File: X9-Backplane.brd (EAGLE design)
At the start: 122.1 x 89.3 mm, 11 parts

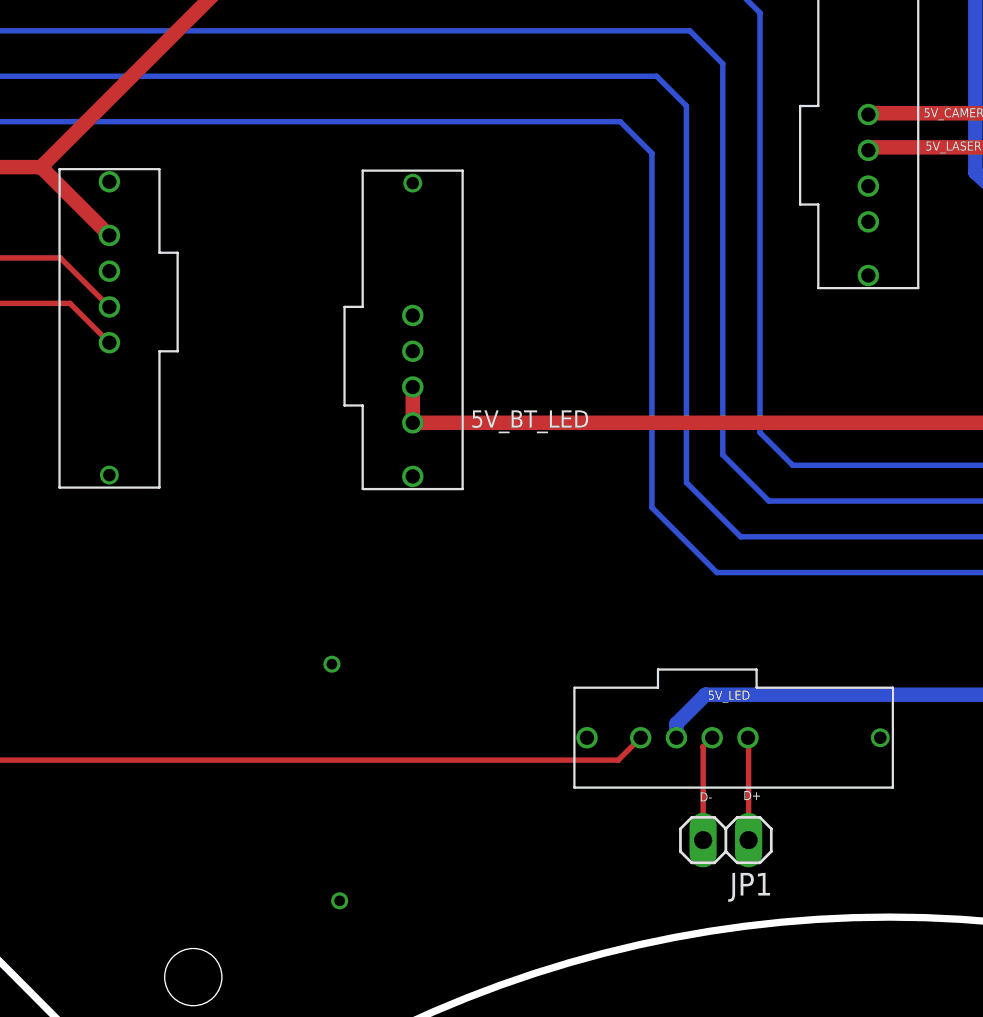
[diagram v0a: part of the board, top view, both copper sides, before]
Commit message: added debugging pins
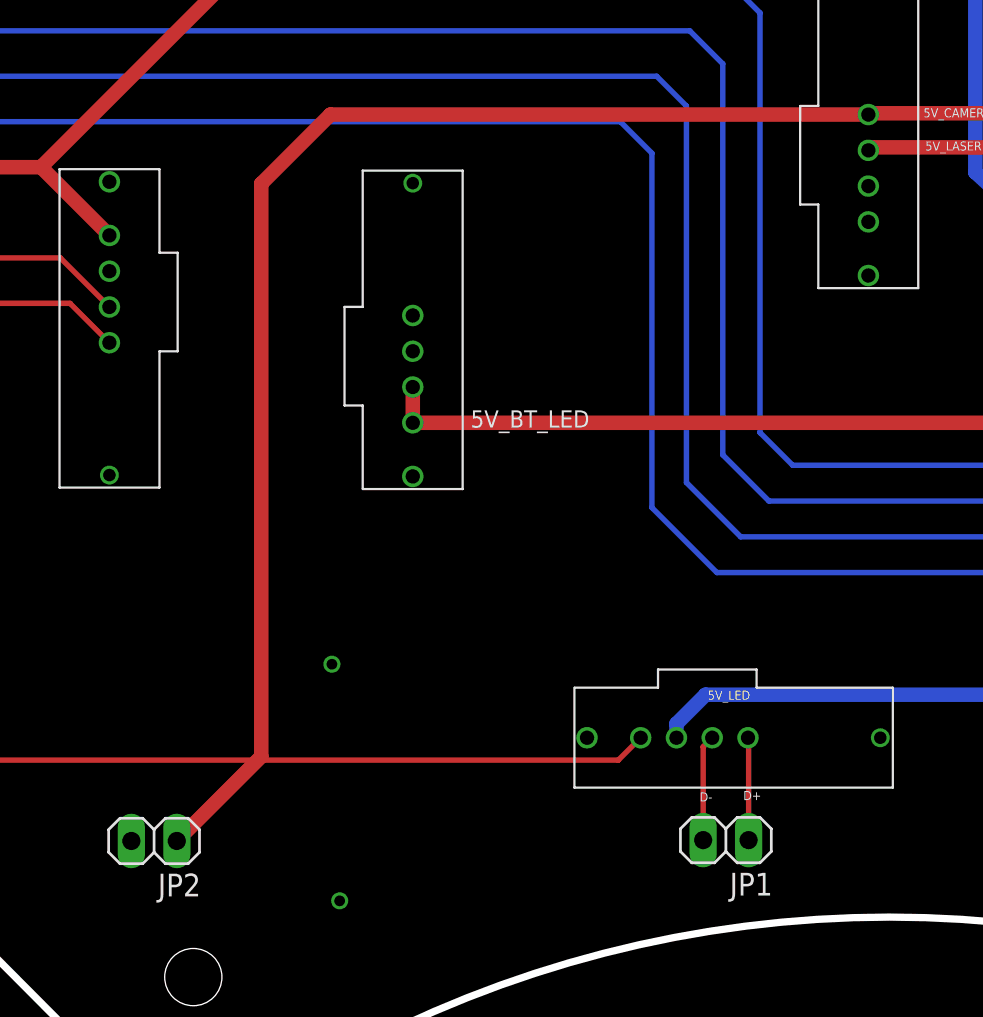
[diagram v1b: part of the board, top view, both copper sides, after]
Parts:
- added JP2: (no value), pinhead:1X02
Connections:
- net 5V_CAMERA_TUBE: now also JP2.1
- net GND: now also JP2.2
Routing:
- net 5V_CAMERA_TUBE: track 68.2 -> 142.5 mm
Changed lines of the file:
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@@
 <text x="103.8" y="63.9" size="1.778" layer="22" rot="MR0">MAIN_POWER</text>
 <wire x1="121.510525" y1="62.19769375" x2="121.485125" y2="12.1368625" width="0.4064" layer="20"/>
-<text x="41.8248" y="27.3338" size="1.778" layer="22" rot="MR0">BT_POWER</text>
-<text x="22.5962" y="27.0222" size="1.778" layer="22" rot="MR0">BT_SIGNAL</text>
-<text x="69.881" y="25.9566" size="1.778" layer="22" rot="MR0">CAMPOW</text>
+<text x="41.266" y="23.5492" size="1.778" layer="22" rot="MR0">BT_POWER</text>
+<text x="22.774" y="23.7964" size="1.778" layer="22" rot="MR0">BT_SIGNAL</text>
+<text x="65.9186" y="35.0244" size="1.778" layer="22" rot="MR0">CAMPOW</text>
 <text x="71.1874" y="11.2268" size="1.778" layer="22" rot="MR0">CAMDATA</text>
 <text x="41.2954" y="78.4302" size="1.778" layer="22" rot="MR0">S_PIEZO</text>
@@
 <element name="JP1" library="pinhead" package="1X02" value="" x="52.0652" y="6.5744" rot="R180"/>
 <element name="PS" library="con-hirose-df13" package="DF13-4P-1.25DSA" value="DF13-4P-1.25DSA" x="61.018" y="77.5974" rot="R90"/>
+<element name="JP2" library="pinhead" package="1X02" value="" x="20.0914" y="6.5278" rot="R180"/>
 </elements>
 <signals>
@@
 <via x="20.805134375" y="58.000896875" extent="1-16" drill="0.6"/>
 <via x="16.187415625" y="69.552815625" extent="1-16" drill="0.6"/>
+<contactref element="JP2" pad="2"/>
 </signal>
 <signal name="N$11">
@@
 <wire x1="68.4022" y1="47.2186" x2="60.105" y2="47.2186" width="0.8128" layer="1"/>
 <wire x1="60.105" y1="47.2186" x2="60.033759375" y2="47.147359375" width="0.8128" layer="1"/>
+<contactref element="JP2" pad="1"/>
+<wire x1="60.033759375" y1="47.147359375" x2="29.951559375" y2="47.147359375" width="0.8128" layer="1"/>
+<wire x1="29.951559375" y1="47.147359375" x2="26.0858" y2="43.2816" width="0.8128" layer="1"/>
+<wire x1="26.0858" y1="43.2816" x2="26.0858" y2="11.2522" width="0.8128" layer="1"/>
+<wire x1="26.0858" y1="11.2522" x2="21.3614" y2="6.5278" width="0.8128" layer="1"/>
 </signal>
 <signal name="5V_BT_LED">

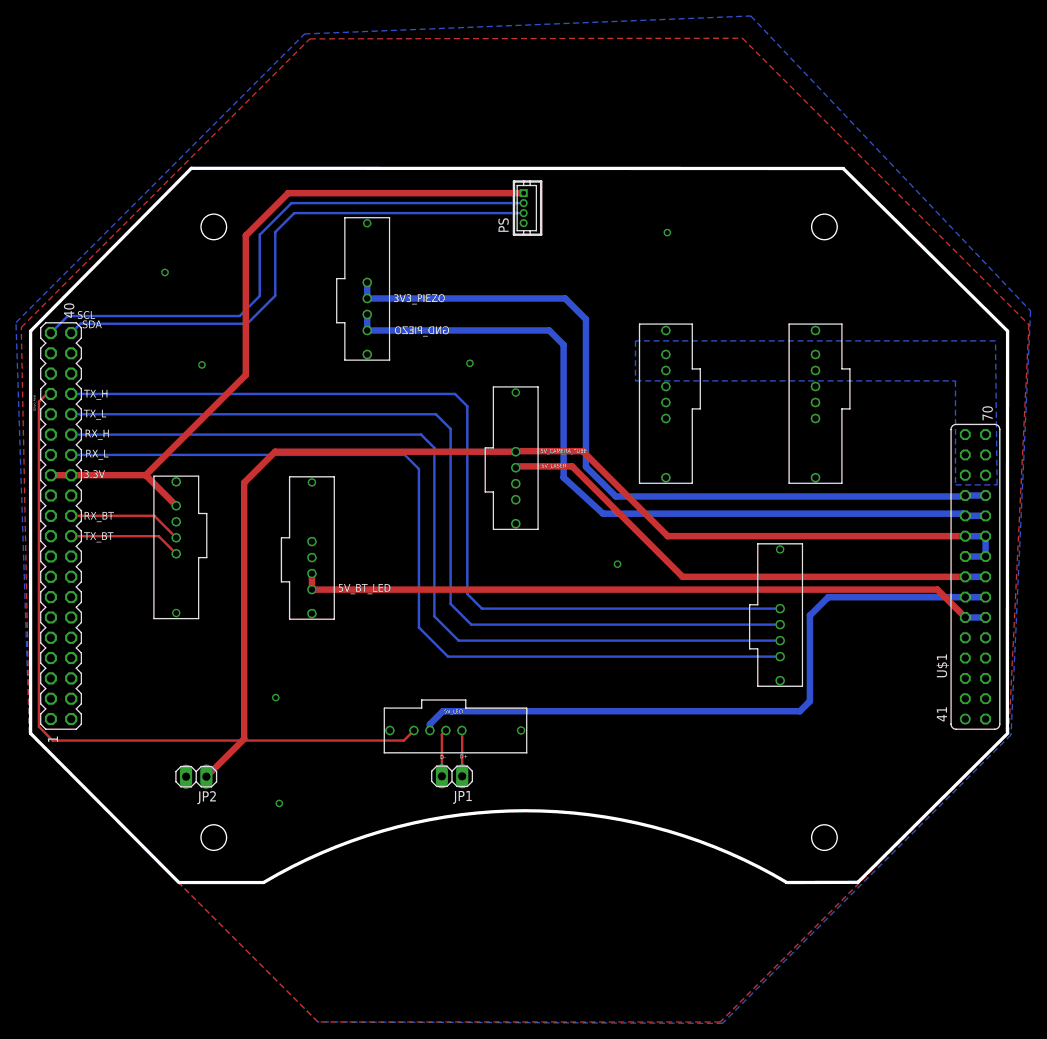
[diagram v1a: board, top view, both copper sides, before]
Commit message: Fixed routing issue
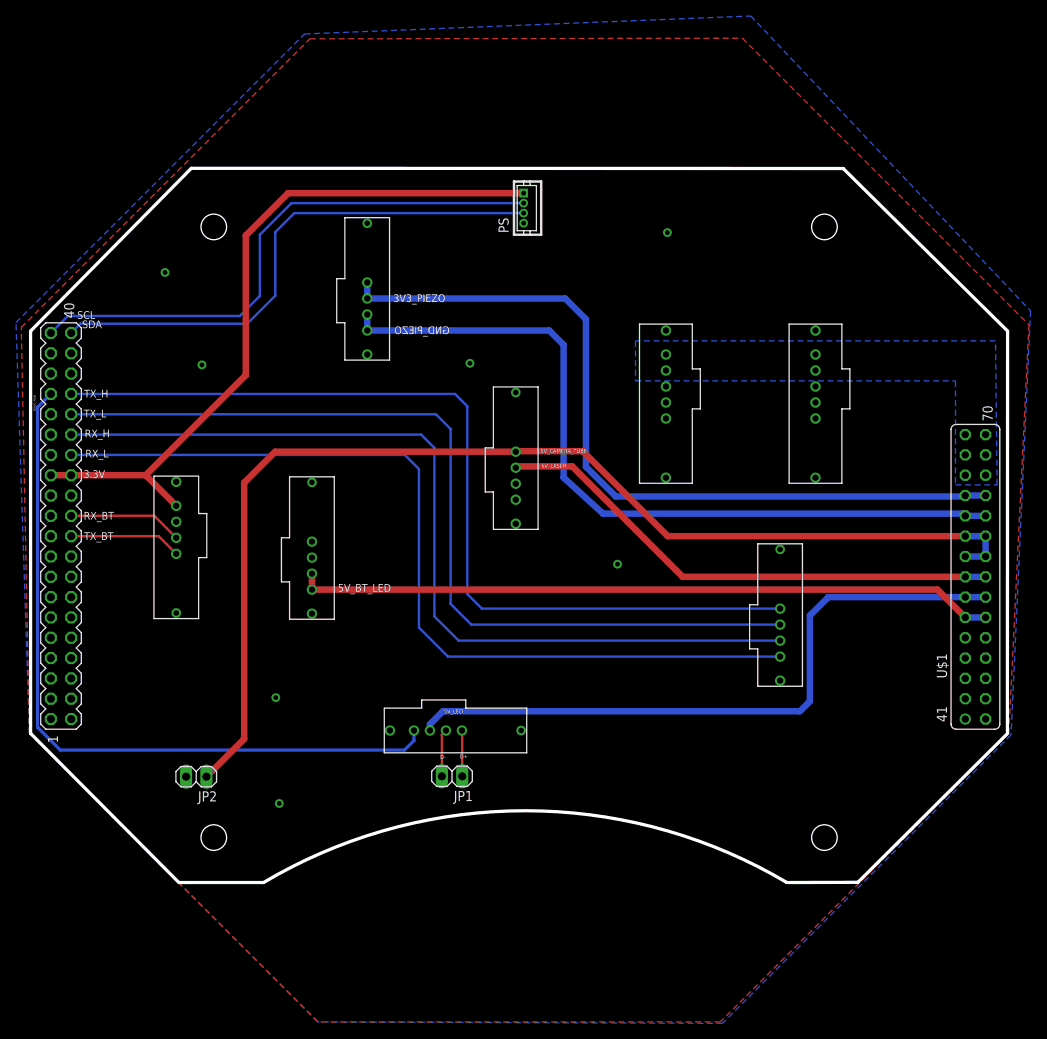
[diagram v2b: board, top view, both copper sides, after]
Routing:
- net SERVO_PWM: track 90.6 -> 92.3 mm
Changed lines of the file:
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@@
 <setting verticaltext="up"/>
 </settings>
-<grid distance="1" unitdist="mil" unit="mil" style="lines" multiple="1" display="yes" altdistance="0.025" altunitdist="inch" altunit="inch"/>
+<grid distance="10" unitdist="mil" unit="mil" style="lines" multiple="1" display="yes" altdistance="0.025" altunitdist="inch" altunit="inch"/>
 <layers>
 <layer number="1" name="Top" color="4" fill="1" visible="yes" active="yes"/>
@@
 </class>
 </classes>
-<designrules name="LaenPCBOrder">
-<description language="de">&lt;b&gt;EAGLE Design Rules&lt;/b&gt;
+<designrules name="GoldPhoenix">
+<description language="en">
+&lt;b&gt;Gold Phoenix PCB Design Rules&lt;/b&gt;
 &lt;p&gt;
-Die Standard-Design-Rules sind so gewählt, dass sie für
-die meisten Anwendungen passen. Sollte ihre Platine
-besondere Anforderungen haben, treffen Sie die erforderlichen
-Einstellungen hier und speichern die Design Rules unter
-einem neuen Namen ab.</description>
-<description language="en">&lt;b&gt;Laen's PCB Order Design Rules&lt;/b&gt;
-&lt;p&gt;
-Please make sure your boards conform to these design rules.</description>
+Created by Nick Molo for the Purdue IEEE ROV Team
+</description>
 <param name="layerSetup" value="(1*16)"/>
-<param name="mtCopper" value="0.0356mm 0.0356mm 0.0356mm 0.0356mm 0.0356mm 0.0356mm 0.0356mm 0.0356mm 0.0356mm 0.0356mm 0.0356mm 0.0356mm 0.0356mm 0.0356mm 0.0356mm 0.0356mm"/>
-<param name="mtIsolate" value="1.5011mm 0.1499mm 0.2007mm 0.1499mm 0.2007mm 0.1499mm 0.2007mm 0.1499mm 0.2007mm 0.1499mm 0.2007mm 0.1499mm 0.2007mm 0.1499mm 0.2007mm"/>
-<param name="mdWireWire" value="6mil"/>
-<param name="mdWirePad" value="6mil"/>
-<param name="mdWireVia" value="6mil"/>
-<param name="mdPadPad" value="6mil"/>
-<param name="mdPadVia" value="6mil"/>
-<param name="mdViaVia" value="6mil"/>
-<param name="mdSmdPad" value="6mil"/>
-<param name="mdSmdVia" value="6mil"/>
-<param name="mdSmdSmd" value="6mil"/>
+<param name="mtCopper" value="0.035mm 0.035mm 0.035mm 0.035mm 0.035mm 0.035mm 0.035mm 0.035mm 0.035mm 0.035mm 0.035mm 0.035mm 0.035mm 0.035mm 0.035mm 0.035mm"/>
+<param name="mtIsolate" value="1.5mm 0.15mm 0.2mm 0.15mm 0.2mm 0.15mm 0.2mm 0.15mm 0.2mm 0.15mm 0.2mm 0.15mm 0.2mm 0.15mm 0.2mm"/>
+<param name="mdWireWire" value="7mil"/>
+<param name="mdWirePad" value="7mil"/>
+<param name="mdWireVia" value="7mil"/>
+<param name="mdPadPad" value="7mil"/>
+<param name="mdPadVia" value="7mil"/>
+<param name="mdViaVia" value="7mil"/>
+<param name="mdSmdPad" value="7mil"/>
+<param name="mdSmdVia" value="7mil"/>
+<param name="mdSmdSmd" value="7mil"/>
 <param name="mdViaViaSameLayer" value="8mil"/>
 <param name="mnLayersViaInSmd" value="2"/>
-<param name="mdCopperDimension" value="15mil"/>
-<param name="mdDrill" value="6mil"/>
+<param name="mdCopperDimension" value="10mil"/>
+<param name="mdDrill" value="8mil"/>
 <param name="mdSmdStop" value="0mil"/>
-<param name="msWidth" value="6mil"/>
-<param name="msDrill" value="13mil"/>
-<param name="msMicroVia" value="13mil"/>
+<param name="msWidth" value="7mil"/>
+<param name="msDrill" value="10mil"/>
+<param name="msMicroVia" value="9.99mm"/>
 <param name="msBlindViaRatio" value="0.5"/>
 <param name="rvPadTop" value="0.25"/>
@@
 <param name="rvMicroViaOuter" value="0.25"/>
 <param name="rvMicroViaInner" value="0.25"/>
-<param name="rlMinPadTop" value="7mil"/>
+<param name="rlMinPadTop" value="10mil"/>
 <param name="rlMaxPadTop" value="20mil"/>
-<param name="rlMinPadInner" value="7mil"/>
+<param name="rlMinPadInner" value="10mil"/>
 <param name="rlMaxPadInner" value="20mil"/>
-<param name="rlMinPadBottom" value="7mil"/>
+<param name="rlMinPadBottom" value="10mil"/>
 <param name="rlMaxPadBottom" value="20mil"/>
-<param name="rlMinViaOuter" value="7mil"/>
+<param name="rlMinViaOuter" value="10mil"/>
 <param name="rlMaxViaOuter" value="20mil"/>
-<param name="rlMinViaInner" value="7mil"/>
+<param name="rlMinViaInner" value="10mil"/>
 <param name="rlMaxViaInner" value="20mil"/>
 <param name="rlMinMicroViaOuter" value="4mil"/>
@@
 <param name="mvStopFrame" value="1"/>
 <param name="mvCreamFrame" value="0"/>
-<param name="mlMinStopFrame" value="3mil"/>
-<param name="mlMaxStopFrame" value="3mil"/>
+<param name="mlMinStopFrame" value="4mil"/>
+<param name="mlMaxStopFrame" value="4mil"/>
 <param name="mlMinCreamFrame" value="0mil"/>
 <param name="mlMaxCreamFrame" value="0mil"/>
-<param name="mlViaStopLimit" value="0mil"/>
+<param name="mlViaStopLimit" value="25mil"/>
 <param name="srRoundness" value="0"/>
 <param name="srMinRoundness" value="0mil"/>
@@
 <contactref element="U$1" pad="33"/>
 <contactref element="CAMDATA" pad="4"/>
-<wire x1="1.92" y1="54.37" x2="1.411" y2="54.37" width="0.3048" layer="1"/>
-<wire x1="1.411" y1="54.37" x2="0.4318" y2="53.3908" width="0.3048" layer="1"/>
-<wire x1="0.4318" y1="53.3908" x2="0.4318" y2="12.7762" width="0.3048" layer="1"/>
-<wire x1="0.4318" y1="12.7762" x2="2.1336" y2="11.049" width="0.3048" layer="1"/>
-<wire x1="2.1336" y1="11.049" x2="46.0516" y2="11.049" width="0.3048" layer="1"/>
-<wire x1="46.0516" y1="11.049" x2="47.302" y2="12.2994" width="0.3048" layer="1"/>
+<wire x1="47.302" y1="12.2994" x2="47.302" y2="11.0308" width="0.4064" layer="16"/>
+<wire x1="47.302" y1="11.0308" x2="46.1264" y2="9.8552" width="0.4064" layer="16"/>
+<wire x1="46.1264" y1="9.8552" x2="3.0988" y2="9.8552" width="0.4064" layer="16"/>
+<wire x1="3.0988" y1="9.8552" x2="0.254" y2="12.7" width="0.4064" layer="16"/>
+<wire x1="0.254" y1="12.7" x2="0.254" y2="52.704" width="0.4064" layer="16"/>
+<wire x1="0.254" y1="52.704" x2="1.92" y2="54.37" width="0.4064" layer="16"/>
 </signal>
 <signal name="+12V">
